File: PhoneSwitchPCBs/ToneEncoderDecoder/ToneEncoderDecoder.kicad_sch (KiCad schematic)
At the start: 13 parts

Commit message: More work on Tone Gen/Decoder schematic
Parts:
- removed C?: 30p, symbol Device:C_Small
- removed C? (x2): .1u, symbol Device:C_Small
- removed IC?: XRA1403IG24TR-F, SOP65P640X120-24N, symbol SamacSys_Parts:XRA1403IG24TR-F
- removed IC? (x2): MT8870DN1, SOP65P780X200-20N, symbol SamacSys_Parts:MT8870DN1
- removed R? (x6): 100K, symbol Device:R_Small
- removed Y?: 3.579545MHz, symbol Device:Crystal_Small
- added C? (x16): .1u, Capacitor_SMD:C_1206_3216Metric_Pad1.33x1.80mm_HandSolder, symbol Device:C_Small
- added C? (x19): .1u, Capacitor_SMD:C_0603_1608Metric_Pad1.08x0.95mm_HandSolder, symbol Device:C_Small
- added C? (x6): 2.2u, Capacitor_THT:CP_Radial_D6.3mm_P2.50mm, symbol Device:C_Small
- added C?: 30p, Capacitor_SMD:C_0603_1608Metric_Pad1.08x0.95mm_HandSolder, symbol Device:C_Small
- added D? (x11): PMBD7000, Package_TO_SOT_SMD:SOT-23, symbol SwitchBackplaneParts:PMBD7000
- added IC?: NXB0108PWJ, SOP65P640X110-20N, symbol SamacSys_Parts:NXB0108PWJ
- added R? (x8): 4.7k, Resistor_SMD:R_0805_2012Metric_Pad1.20x1.40mm_HandSolder, symbol Device:R_Small
- added R? (x4): 2.55k, Resistor_SMD:R_0805_2012Metric_Pad1.20x1.40mm_HandSolder, symbol Device:R_Small
- added R? (x14): 100k, Resistor_SMD:R_0805_2012Metric_Pad1.20x1.40mm_HandSolder, symbol Device:R_Small
- added R? (x4): 3.6k, Resistor_SMD:R_0805_2012Metric_Pad1.20x1.40mm_HandSolder, symbol Device:R_Small
- added R? (x8): 2.2k, Resistor_SMD:R_0805_2012Metric_Pad1.20x1.40mm_HandSolder, symbol Device:R_Small
- added R? (x4): 3.32k, Resistor_SMD:R_0805_2012Metric_Pad1.20x1.40mm_HandSolder, symbol Device:R_Small
- added R? (x2): 300k, Resistor_SMD:R_0805_2012Metric_Pad1.20x1.40mm_HandSolder, symbol Device:R_Small
- added R? (x4): 4.53k, Resistor_SMD:R_0805_2012Metric_Pad1.20x1.40mm_HandSolder, symbol Device:R_Small
- added RV? (x2): 500k, Imported_Parts:TC33X-2_1, symbol Device:R_POT_Small
- added U? (x10): TL074, Package_SO:SOIC-14_3.9x8.7mm_P1.27mm, symbol Amplifier_Operational:TL074
- added U? (x2): MT8870DS1, Package_SO:SOIC-18W_7.5x11.6mm_P1.27mm, symbol Imported_Parts:MT8870DS1
- added U? (x3): TL072, symbol Amplifier_Operational:TL072
- added U? (x10): 74HC4316, Package_SO:SO-16_3.9x9.9mm_P1.27mm, symbol SwitchBackplaneParts:74HC4316
- added U?: XRA1403IG24TR-F, Package_SO:TSSOP-24_4.4x7.8mm_P0.65mm, symbol Imported_Parts:XRA1403IG24TR-F
- added Y?: 3.579545 MHz, Crystal:Crystal_SMD_HC49-SD_HandSoldering, symbol Device:Crystal_Small
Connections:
- net +3V3: now also C?.1, C?.1, IC?.10 (OE), IC?.2 (VCC(A)), U?.24 (VCC)
- net GND: now also C?.1, C?.1, C?.1, C?.1, C?.1, C?.1, C?.1, C?.1, C?.1, C?.1, C?.1, C?.1, C?.1, C?.1, C?.1, C?.1, C?.1, C?.2, C?.2, C?.2, C?.2, C?.2, C?.2, C?.2, C?.2, C?.2, C?.2, C?.2, IC?.11 (GND), R?.1, R?.1, R?.1, R?.1, R?.1, R?.1, R?.1, R?.1, R?.1, R?.1, R?.1, R?.1, R?.1, R?.1, R?.1, R?.1, U?.12 (GND), U?.3 (+), U?.5 (+), U?.5 (INH), U?.5 (INH), U?.6 (PWDN), U?.6 (PWDN), U?.7 (E), U?.7 (E), U?.8 (GND), U?.8 (GND), U?.9 (VSS), U?.9 (VSS)
- new net: C?.2, C?.2, R?.2, U?.12 (+) (x2)
- new net: C?.2, C?.2, R?.2, U?.5 (+) (x2)
- new net: D?.3 (K1A2), R?.2, R?.2, U?.13 (-) (x2)
- new net: D?.1 (A1), D?.2 (K2), R?.1, R?.1, R?.2, U?.14 (x2)
- new net: D?.1 (A1), D?.2 (K2), R?.1, R?.1, R?.2, U?.1 (x2)
- new net: D?.3 (K1A2), R?.2, R?.2, U?.2 (-) (x2)
- new net: R?.1, U?.10 (x2)
- new net: D?.1 (A1), D?.2 (K2), R?.1, R?.1, R?.2, U?.8 (x2)
- new net: C?.2, C?.2, R?.2, U?.3 (+) (x2)
- new net: U?.1 (IN+), U?.4 (VREF) (x2)
- new net: R?.1, U?.16 (EST) (x2)
- new net: C?.2, R?.2, U?.17 (ST/GT) (x2)
- new net: R?.1, R?.2, U?.2 (IN-) (x2)
- new net: R?.2, U?.3 (GS) (x2)
- new net: C?.1, U?.7 (OSC1)
- new net: D?.3 (K1A2), R?.2, R?.2, U?.6 (-) (x2)
- new net: C?.1, R?.2 (x8)
- new net: R?.2, U?.11, U?.12, U?.2, U?.3 (x2)
- new net: R?.1, U?.13 (x2)
- new net: R?.1, U?.4 (x2)
- new net: D?.1 (A1), D?.2 (K2), R?.1, R?.1, R?.2, U?.7 (x2)
- new net: R?.1, U?.1 (x2)
- new net: C?.2, C?.2, R?.2, U?.10 (+) (x2)
- new net: C?.1, D?.3 (K1A2)
- new net: D?.3 (K1A2), R?.2, R?.2, U?.9 (-) (x2)
- new net: C?.2, U?.8 (OSC2), Y?.2
- new net: R?.1, RV?.3, U?.6 (-)
- new net: IC?.1 (A1), U?.4 (P0)
- new net: IC?.3 (A2), U?.5 (P1)
- new net: IC?.4 (A3), U?.6 (P2)
- new net: IC?.5 (A4), U?.7 (P3)
- new net: IC?.6 (A5), U?.8 (P4)
- new net: IC?.7 (A6), U?.9 (P5)
- new net: IC?.8 (A7), U?.10 (P6)
- new net: IC?.9 (A8), U?.11 (P7)
- new net: R?.1, RV?.3, U?.2 (-)
- new net: U?.7 (OSC1), Y?.1
- new net +5VA: C?.1, C?.1, C?.1, C?.1, C?.1, C?.1, D?.2 (K2), D?.2 (K2), D?.2 (K2), U?.16 (V+), U?.16 (V+), U?.4 (V+), U?.4 (V+), U?.8 (V+)
- new net +5VD: C?.1, C?.1, C?.1, C?.1, C?.1, IC?.19 (VCC(B)), U?.10 (TOE), U?.10 (TOE), U?.18 (VDD), U?.18 (VDD)
- new net -5VA: C?.2, C?.2, C?.2, C?.2, C?.2, C?.2, D?.1 (A1), D?.1 (A1), D?.1 (A1), U?.11 (V-), U?.11 (V-), U?.4 (V-), U?.9 (V-), U?.9 (V-)
- new net 350A: IC?.20 (B1), U?.15
- new net 350B: IC?.15 (B5), U?.15
- new net 440A: IC?.18 (B2), U?.5
- new net 440B: IC?.14 (B6), U?.5
- new net 480A: IC?.17 (B3), U?.6
- new net 480B: IC?.13 (B7), U?.6
- new net 620A: IC?.16 (B4), U?.14
- new net 620B: IC?.12 (B8), U?.14
- new net CST: U?.21 (CS#)
- new net DA1: U?.11 (Q1), U?.13 (P8)
- new net DA2: U?.12 (Q2), U?.14 (P9)
- new net DA3: U?.13 (Q3), U?.15 (P10)
- new net DA4: U?.14 (Q4), U?.16 (P11)
- new net DB1: U?.11 (Q1), U?.17 (P12)
- new net DB2: U?.12 (Q2), U?.18 (P13)
- new net DB3: U?.13 (Q3), U?.19 (P14)
- new net DB4: U?.14 (Q4), U?.20 (P15)
- new net DH1: U?.15 (STD)
- new net DH2: U?.15 (STD)
- new net MISO: U?.23 (SO)
- new net MOSI: U?.2 (SI)
- new net SCK: U?.22 (SCL)
- new net T1: C?.1, D?.3 (K1A2), R?.1, RV?.1, RV?.2, U?.1
- new net T1R: C?.2, C?.2
- new net T1T: C?.2, C?.2
- new net T2: C?.1, D?.3 (K1A2), R?.1, RV?.1, RV?.2, U?.7
- new net T2R: C?.2
- new net T2T: C?.2
- no-connect marks 5 -> 3

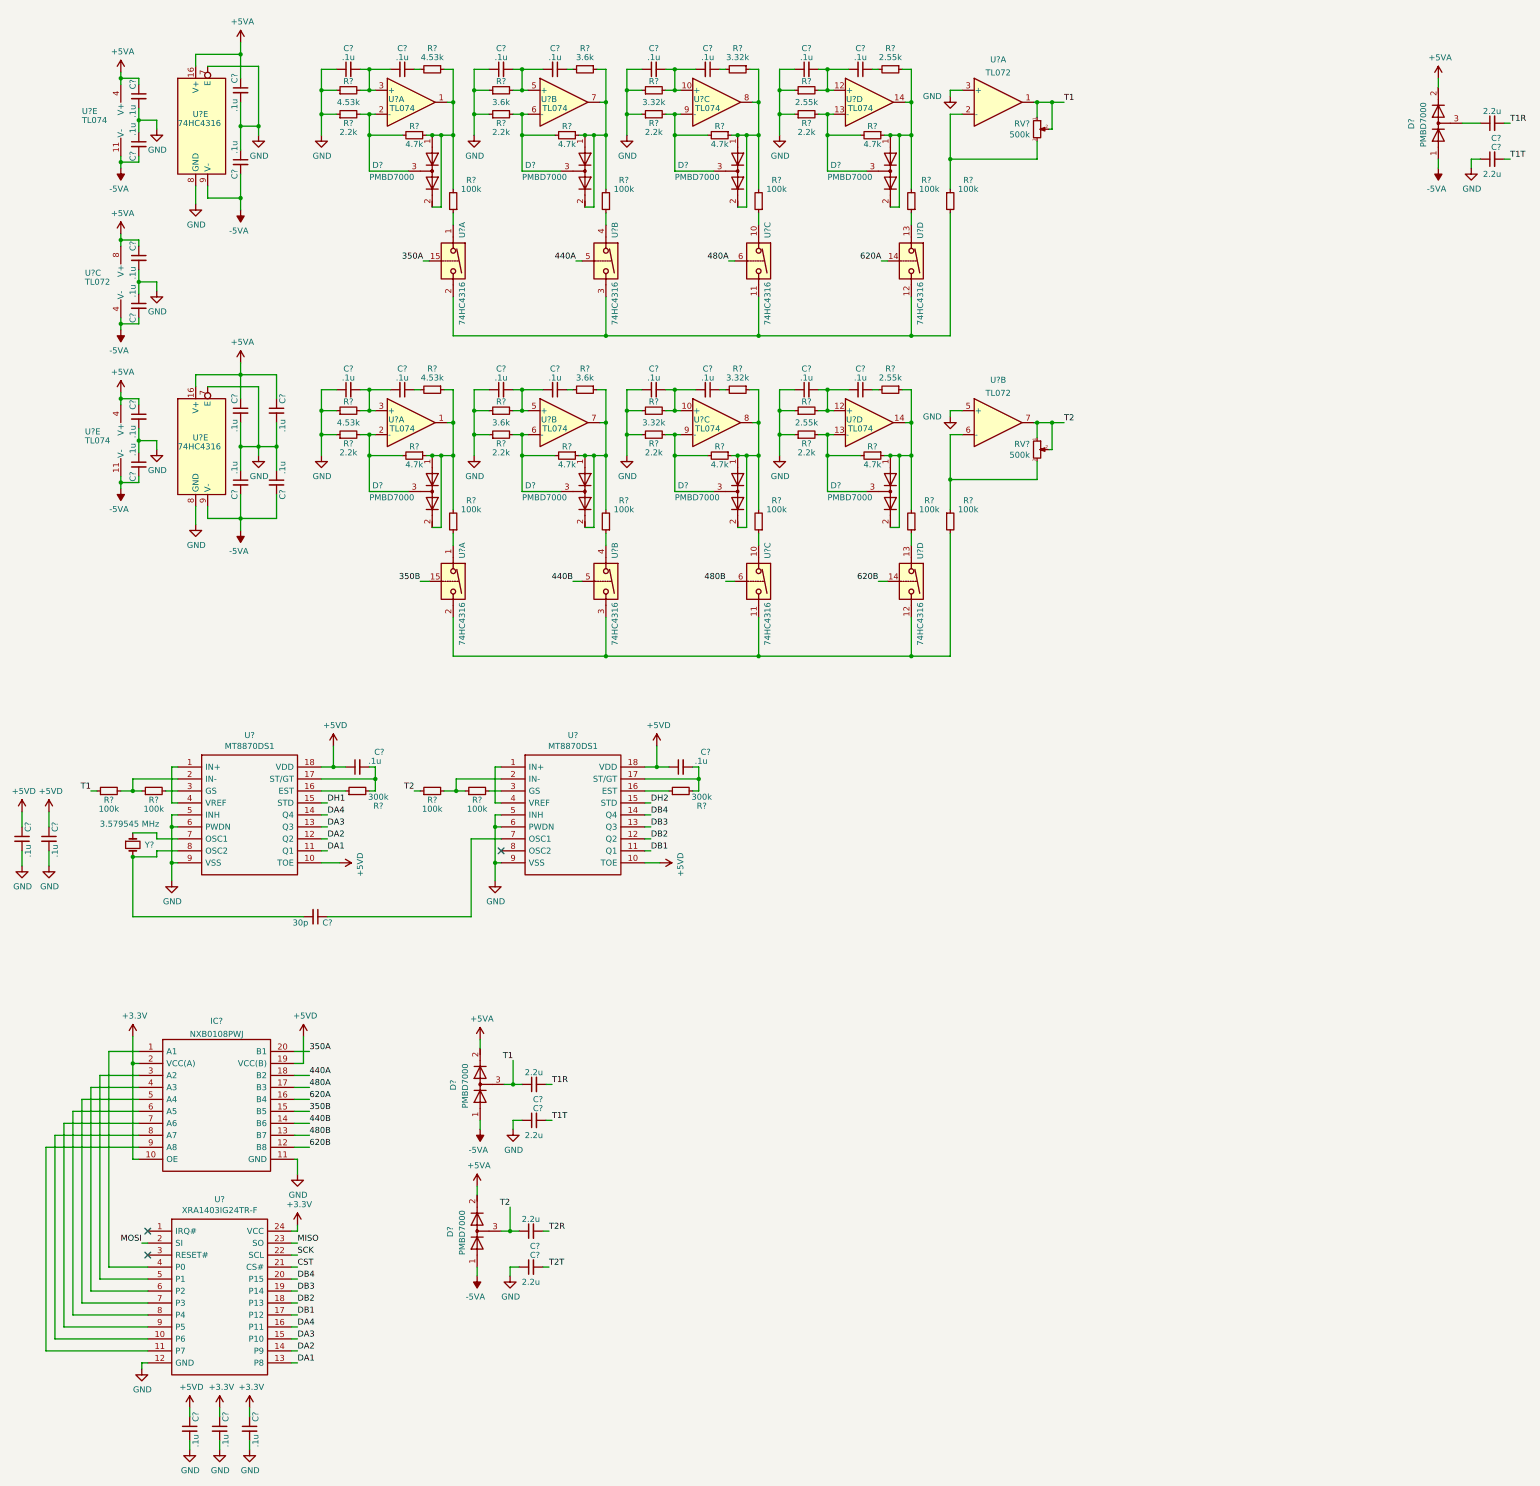
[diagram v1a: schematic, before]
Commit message: Finish? Tone Generator / Decoder Schematic
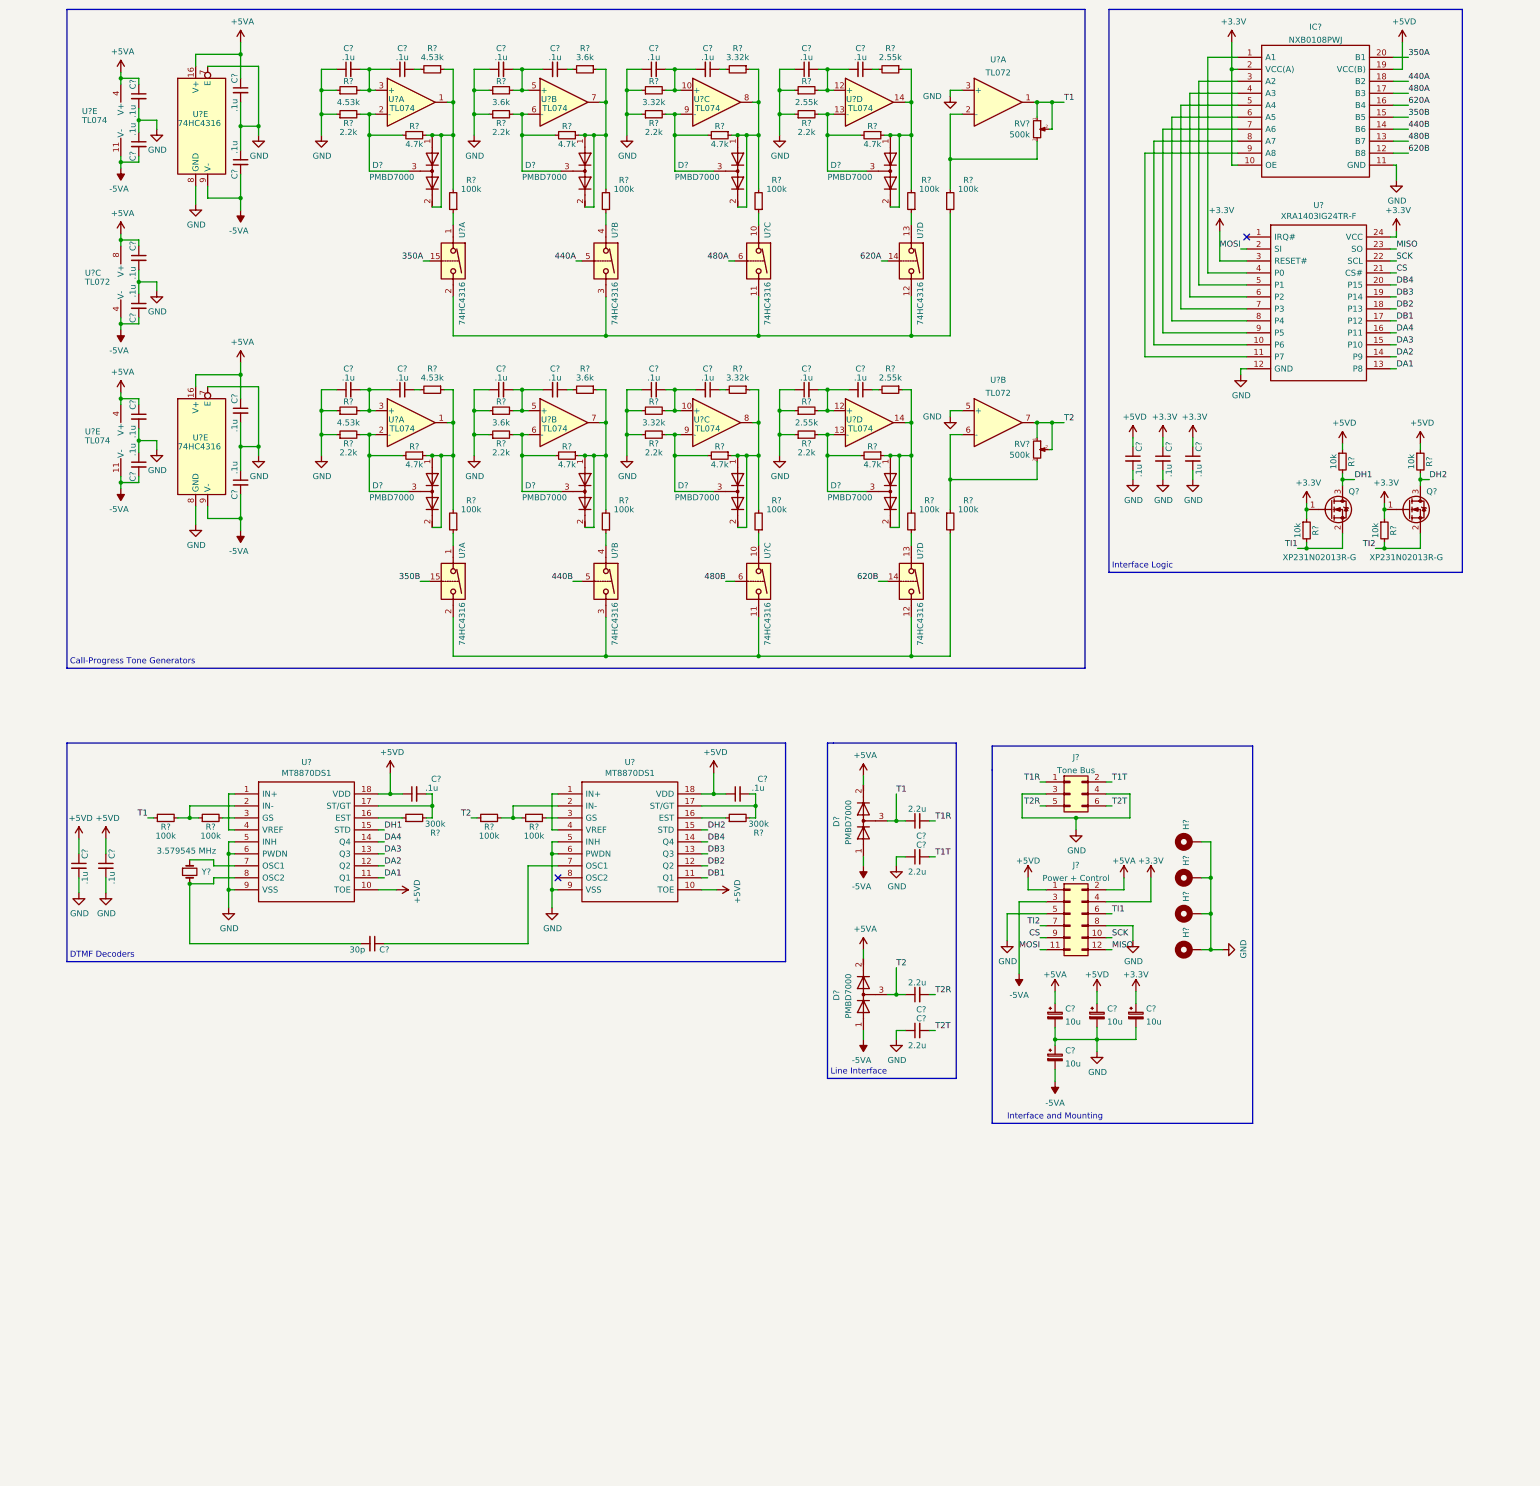
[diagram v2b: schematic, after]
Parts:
- removed C? (x4): 2.2u, Capacitor_THT:CP_Radial_D6.3mm_P2.50mm, symbol Device:C_Small
- removed C? (x2): .1u, Capacitor_SMD:C_0603_1608Metric_Pad1.08x0.95mm_HandSolder, symbol Device:C_Small
- removed D? (x2): PMBD7000, Package_TO_SOT_SMD:SOT-23, symbol SwitchBackplaneParts:PMBD7000
- added C? (x4): 10u, symbol Device:C_Polarized_Small
- added C? (x2): 2.2u, Capacitor_THT:CP_Radial_D6.3mm_P2.50mm, symbol Device:C_Small
- added D?: PMBD7000, Package_TO_SOT_SMD:SOT-23, symbol SwitchBackplaneParts:PMBD7000
- added H? (x4): M3, symbol Mechanical:MountingHole_Pad
- added J?: Tone Bus, symbol Connector_Generic:Conn_02x03_Odd_Even
- added J?: Power + Control, symbol Connector_Generic:Conn_02x06_Odd_Even
- added Q? (x2): XP231N02013R-G, Package_TO_SOT_SMD:SOT-323_SC-70_Handsoldering, symbol PhoneInterfaceParts:XP231N02013R-G
- added R? (x4): 10k, Resistor_SMD:R_0805_2012Metric_Pad1.20x1.40mm_HandSolder, symbol Device:R_Small
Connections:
- net +3V3: now also U?.3 (RESET#), C?.1, J?.4 (Pin_4), Q?.1 (G), Q?.1 (G), R?.1, R?.1
- net +5VA: now also C?.1, D?.2 (K2), J?.2 (Pin_2)
- net +5VD: now also C?.1, J?.1 (Pin_1), R?.1, R?.1
- net -5VA: now also C?.2, D?.1 (A1), J?.3 (Pin_3)
- net DH1: now also Q?.3 (D), R?.2
- net DH2: now also Q?.3 (D), R?.2
- net GND: now also C?.1, C?.1, C?.2, C?.2, C?.2, H?.1, H?.1, H?.1, H?.1, J?.3 (Pin_3), J?.4 (Pin_4), J?.5 (Pin_5), J?.8 (Pin_8)
- net MISO: now also J?.12 (Pin_12)
- net MOSI: now also J?.11 (Pin_11)
- net SCK: now also J?.10 (Pin_10)
- net T1: now also C?.1, D?.3 (K1A2)
- net T1R: now also J?.1 (Pin_1)
- net T1T: now also J?.2 (Pin_2)
- net T2: now also C?.1, D?.3 (K1A2)
- net T2R: now also C?.2, J?.5 (Pin_5)
- net T2T: now also C?.2, J?.6 (Pin_6)
- net CST renamed CS
- net CS: now also J?.9 (Pin_9)
- new net TI1: J?.6 (Pin_6), Q?.2 (S), R?.2
- new net TI2: J?.7 (Pin_7), Q?.2 (S), R?.2
- no-connect marks 3 -> 2
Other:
- note added: "Call-Progress Tone Generators"
- note added: "DTMF Decoders"
- note added: "Interface Logic"
- note added: "Interface and Mounting"
- note added: "Line Interface"
- moved on the sheet: C?, D?, IC?, R?, U?, Y?
